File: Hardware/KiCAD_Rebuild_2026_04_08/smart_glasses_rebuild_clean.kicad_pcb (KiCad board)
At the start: 2 copper layers, 150 x 50 mm, 0 parts

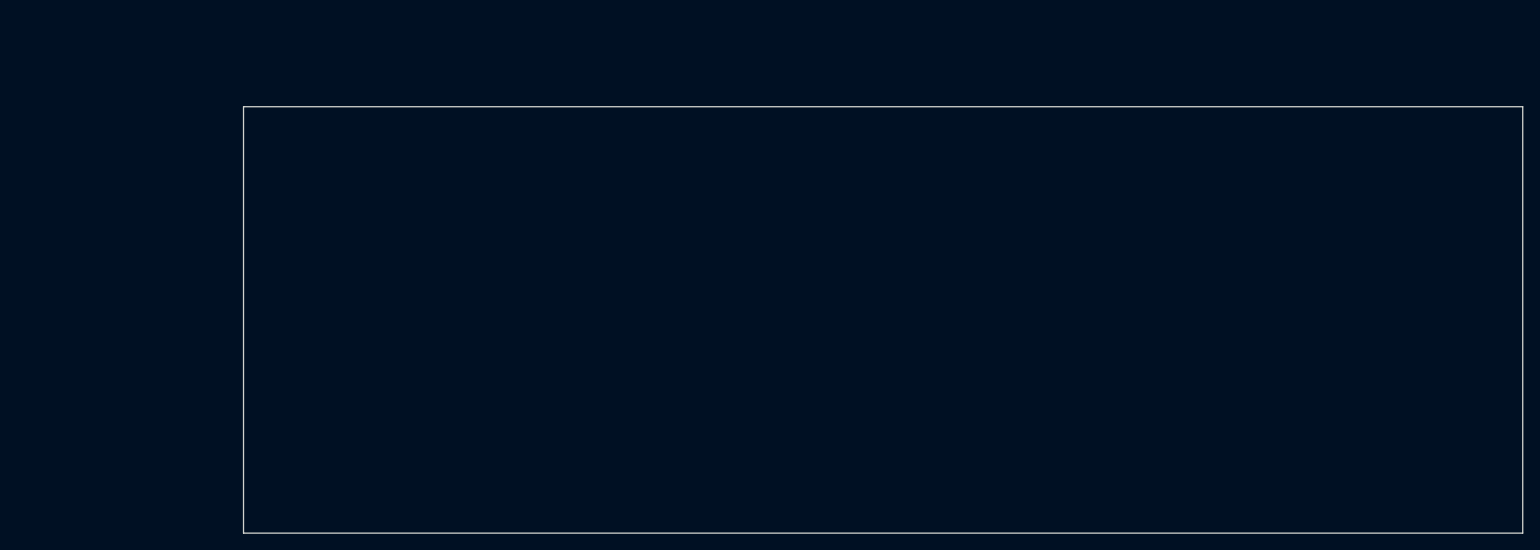
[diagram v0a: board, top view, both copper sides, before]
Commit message: kicad adding button for pwr
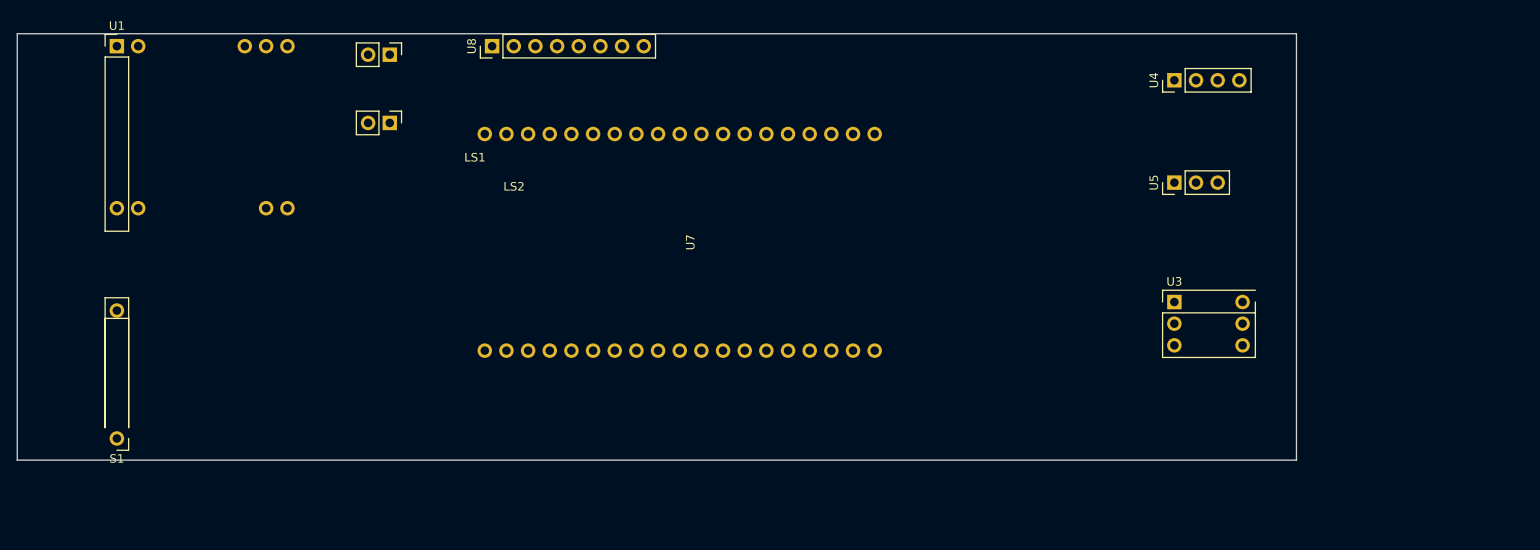
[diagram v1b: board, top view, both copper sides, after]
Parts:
- added LS1: Small Speaker, Connector_PinHeader_2.54mm:PinHeader_1x02_P2.54mm_Vertical, F.Cu at (84.0, 25.0)
- added LS2: Small Speaker, Connector_PinHeader_2.54mm:PinHeader_1x02_P2.54mm_Vertical, F.Cu at (84.0, 33.0)
- added S1: TP4056_BMS, Connector_PinHeader_2.54mm:PinHeader_1x06_P2.54mm_Vertical, F.Cu at (52.0, 70.0)
- added U1: HW-104, Connector_PinHeader_2.54mm:PinHeader_1x09_P2.54mm_Vertical, F.Cu at (52.0, 24.0)
- added U3: INMP441, Connector_PinHeader_2.54mm:PinHeader_1x06_P2.54mm_Vertical, F.Cu at (176.0, 54.0)
- added U4: IIC_OLED, Connector_PinHeader_2.54mm:PinHeader_1x04_P2.54mm_Vertical, F.Cu at (176.0, 28.0)
- added U5: HW-763, Connector_PinHeader_2.54mm:PinHeader_1x03_P2.54mm_Vertical, F.Cu at (176.0, 40.0)
- added U7: ESP32-WROVER-dev, RebuildLib:ESP32_WROVER_DEV_2x19_WIDE, F.Cu at (118.0, 47.0)
- added U8: MPU-6050_Breakout, Connector_PinHeader_2.54mm:PinHeader_1x08_P2.54mm_Vertical, F.Cu at (96.0, 24.0)

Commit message: Kicap Prototype 2 done
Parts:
- added SW1: PWR_SW_LATCH, RebuildLib:Power_Switch_Latching_SPST_2Pin, F.Cu at (64.0, 70.0)
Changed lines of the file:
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@@
 		)
+	)
+	(footprint "RebuildLib:Power_Switch_Latching_SPST_2Pin"
+		(layer "F.Cu")
+		(at 64 70)
+		(descr "Latching SPST power switch, 2-pin THT")
+		(tags "switch latching power spst")
+		(property "Reference" "SW1"
+			(at 3 -3 0)
+			(layer "F.SilkS")
+			(effects
+				(font
+					(size 1 1)
+					(thickness 0.15)
+				)
+			)
+		)
+		(property "Value" "PWR_SW_LATCH"
+			(at 3 3 0)
+			(layer "F.Fab")
+			(effects
+				(font
+					(size 1 1)
+					(thickness 0.15)
+				)
+			)
+		)
+		(property "Datasheet" "~"
+			(at 0 0 0)
+			(layer "F.Fab")
+			(hide yes)
+			(effects
+				(font
+					(size 1 1)
+					(thickness 0.15)
+				)
+			)
+		)
+		(property "Description" "Latching on/off SPST power switch"
+			(at 0 0 0)
+			(layer "F.Fab")
+			(hide yes)
+			(effects
+				(font
+					(size 1 1)
+					(thickness 0.15)
+				)
+			)
+		)
+		(sheetname "/")
+		(sheetfile "smart_glasses_rebuild_clean.kicad_sch")
+		(attr through_hole)
+		(fp_rect
+			(start -2.5 -2)
+			(end 8.5 2)
+			(stroke
+				(width 0.12)
+				(type default)
+			)
+			(fill no)
+			(layer "F.SilkS")
+		)
+		(fp_rect
+			(start -3 -2.5)
+			(end 9 2.5)
+			(stroke
+				(width 0.05)
+				(type default)
+			)
+			(fill no)
+			(layer "F.CrtYd")
+		)
+		(pad "1" thru_hole rect
+			(at 0 0)
+			(size 2.4 2.4)
+			(drill 1.2)
+			(layers "*.Cu" "*.Mask")
+			(remove_unused_layers no)
+			(net 0 "")
+			(pinfunction "1")
+			(pintype "passive")
+		)
+		(pad "2" thru_hole oval
+			(at 6 0)
+			(size 2.4 2.4)
+			(drill 1.2)
+			(layers "*.Cu" "*.Mask")
+			(remove_unused_layers no)
+			(net 0 "")
+			(pinfunction "2")
+			(pintype "passive")
+		)
+		(embedded_fonts no)
 	)
 	(gr_rect
